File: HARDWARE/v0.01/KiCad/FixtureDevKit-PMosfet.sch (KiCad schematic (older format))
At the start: 56 parts, among them J89 FET_0, J90 FET_1, J91 FET_2, J92 FET_3, J93 FET_4, J94 FET_5, J95 FET_6, J96 FET_7, Q10 NTF2955T1G, Q11 NTF2955T1G, Q12 NTF2955T1G, Q5 NTF2955T1G, Q6 NTF2955T1G, Q7 NTF2955T1G, Q8 NTF2955T1G, Q9 NTF2955T1G

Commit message: adjusting page sizes and cleaning up schematics
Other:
- moved on the sheet: J89, J90, J91, J92, J93, J94, J95, J96, Q10, Q11, Q12, Q5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

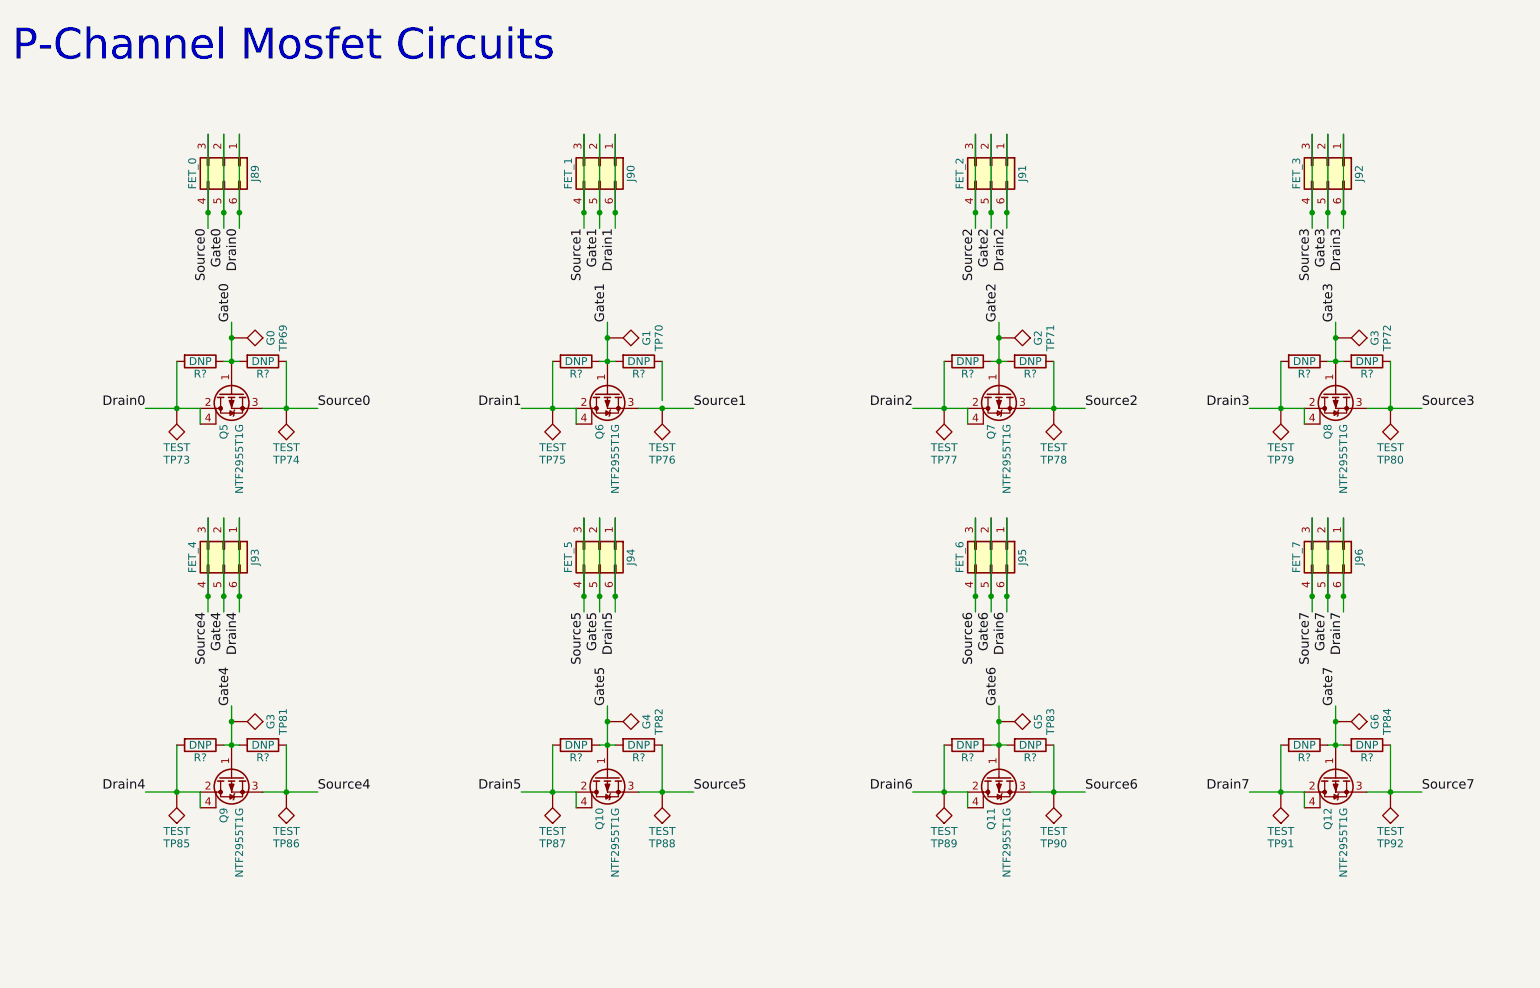
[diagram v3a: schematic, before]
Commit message: cleaning up schematic, run rules check, generate net list
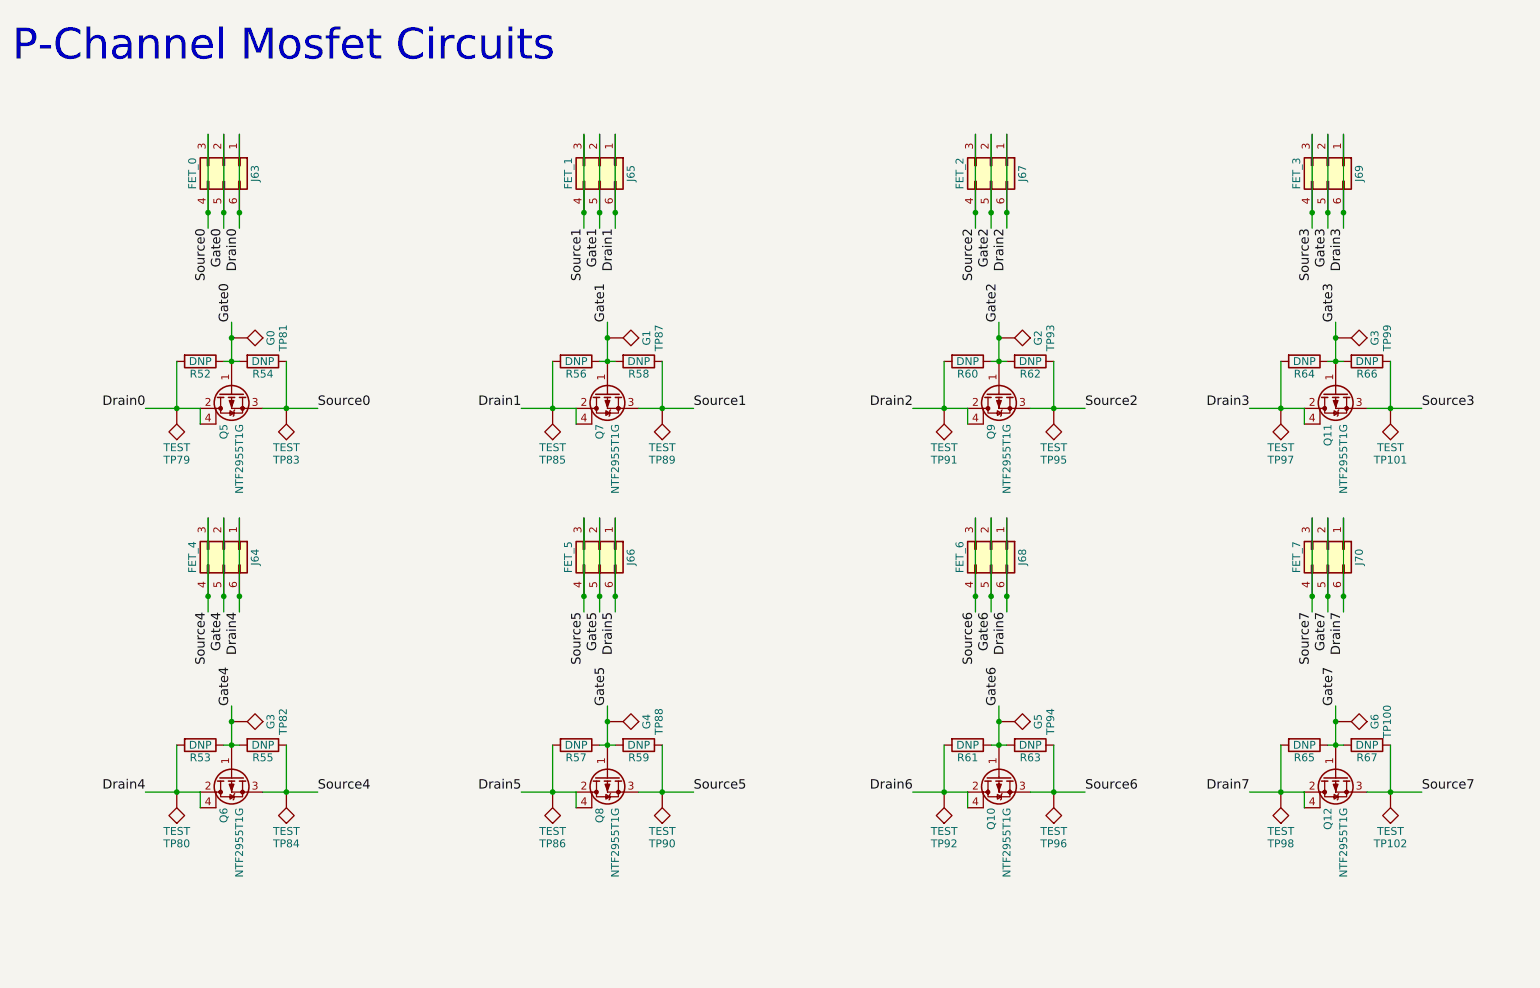
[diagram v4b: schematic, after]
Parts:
- gave numbers to parts that had none: 16
- renumbered J89 to J63, J93 to J64, J90 to J65, J94 to J66, J91 to J67, J95 to J68, J92 to J69, J96 to J70, Q11 to Q10, Q8 to Q11, Q9 to Q6, Q6 to Q7, Q10 to Q8, Q7 to Q9, TP84 to TP100, TP80 to TP101, TP92 to TP102, TP73 to TP79, TP85 to TP80, TP69 to TP81, TP81 to TP82, TP74 to TP83, TP86 to TP84, TP75 to TP85, TP87 to TP86, TP70 to TP87, TP82 to TP88, TP76 to TP89, TP88 to TP90, TP77 to TP91, TP89 to TP92, TP71 to TP93, TP83 to TP94, TP78 to TP95, TP90 to TP96, TP79 to TP97, TP91 to TP98, TP72 to TP99
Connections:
- net Source1: now also R58.1

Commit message: adding footprints
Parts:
- J63, J64, J65, J66, J67, J68, J69, J70: footprint (none) -> Pin_Headers:Pin_Header_Straight_2x03_Pitch2.54mm
- Q10, Q11, Q12, Q5, Q6, Q7, Q8, Q9: footprint (none) -> Pin_Headers:Pin_Header_Straight_1x04_Pitch2.54mm
- R52, R53, R54, R55, R56, R57, R58, R59, R60, R61, R62, R63, R64, R65, R66, R67: footprint (none) -> Resistors_SMD:R_0805_HandSoldering
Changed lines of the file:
@@
 F 0 "R67" V 9330 5150 50  0000 C CNN
 F 1 "DNP" V 9250 5150 50  0000 C CNN
-F 2 "" V 9180 5150 50  0001 C CNN
+F 2 "Resistors_SMD:R_0805_HandSoldering" V 9180 5150 50  0001 C CNN
 F 3 "" H 9250 5150 50  0001 C CNN
 	1    9250 5150
@@
 F 0 "R65" V 8930 5150 50  0000 C CNN
 F 1 "DNP" V 8850 5150 50  0000 C CNN
-F 2 "" V 8780 5150 50  0001 C CNN
+F 2 "Resistors_SMD:R_0805_HandSoldering" V 8780 5150 50  0001 C CNN
 F 3 "" H 8850 5150 50  0001 C CNN
 	1    8850 5150
@@
 F 0 "R61" V 6780 5150 50  0000 C CNN
 F 1 "DNP" V 6700 5150 50  0000 C CNN
-F 2 "" V 6630 5150 50  0001 C CNN
+F 2 "Resistors_SMD:R_0805_HandSoldering" V 6630 5150 50  0001 C CNN
 F 3 "" H 6700 5150 50  0001 C CNN
 	1    6700 5150
@@
 F 0 "R63" V 7180 5150 50  0000 C CNN
 F 1 "DNP" V 7100 5150 50  0000 C CNN
-F 2 "" V 7030 5150 50  0001 C CNN
+F 2 "Resistors_SMD:R_0805_HandSoldering" V 7030 5150 50  0001 C CNN
 F 3 "" H 7100 5150 50  0001 C CNN
 	1    7100 5150
@@
 F 0 "R59" V 4680 5150 50  0000 C CNN
 F 1 "DNP" V 4600 5150 50  0000 C CNN
-F 2 "" V 4530 5150 50  0001 C CNN
+F 2 "Resistors_SMD:R_0805_HandSoldering" V 4530 5150 50  0001 C CNN
 F 3 "" H 4600 5150 50  0001 C CNN
 	1    4600 5150
@@
 F 0 "R57" V 4280 5150 50  0000 C CNN
 F 1 "DNP" V 4200 5150 50  0000 C CNN
-F 2 "" V 4130 5150 50  0001 C CNN
+F 2 "Resistors_SMD:R_0805_HandSoldering" V 4130 5150 50  0001 C CNN
 F 3 "" H 4200 5150 50  0001 C CNN
 	1    4200 5150
@@
 F 0 "R53" V 1880 5150 50  0000 C CNN
 F 1 "DNP" V 1800 5150 50  0000 C CNN
-F 2 "" V 1730 5150 50  0001 C CNN
+F 2 "Resistors_SMD:R_0805_HandSoldering" V 1730 5150 50  0001 C CNN
 F 3 "" H 1800 5150 50  0001 C CNN
 	1    1800 5150
@@
 F 0 "R55" V 2280 5150 50  0000 C CNN
 F 1 "DNP" V 2200 5150 50  0000 C CNN
-F 2 "" V 2130 5150 50  0001 C CNN
+F 2 "Resistors_SMD:R_0805_HandSoldering" V 2130 5150 50  0001 C CNN
 F 3 "" H 2200 5150 50  0001 C CNN
 	1    2200 5150
@@
 F 0 "R66" V 9330 2700 50  0000 C CNN
 F 1 "DNP" V 9250 2700 50  0000 C CNN
-F 2 "" V 9180 2700 50  0001 C CNN
+F 2 "Resistors_SMD:R_0805_HandSoldering" V 9180 2700 50  0001 C CNN
 F 3 "" H 9250 2700 50  0001 C CNN
 	1    9250 2700
@@
 F 0 "R64" V 8930 2700 50  0000 C CNN
 F 1 "DNP" V 8850 2700 50  0000 C CNN
-F 2 "" V 8780 2700 50  0001 C CNN
+F 2 "Resistors_SMD:R_0805_HandSoldering" V 8780 2700 50  0001 C CNN
 F 3 "" H 8850 2700 50  0001 C CNN
 	1    8850 2700
@@
 F 0 "R62" V 7180 2700 50  0000 C CNN
 F 1 "DNP" V 7100 2700 50  0000 C CNN
-F 2 "" V 7030 2700 50  0001 C CNN
+F 2 "Resistors_SMD:R_0805_HandSoldering" V 7030 2700 50  0001 C CNN
 F 3 "" H 7100 2700 50  0001 C CNN
 	1    7100 2700
@@
 F 0 "R60" V 6780 2700 50  0000 C CNN
 F 1 "DNP" V 6700 2700 50  0000 C CNN
-F 2 "" V 6630 2700 50  0001 C CNN
+F 2 "Resistors_SMD:R_0805_HandSoldering" V 6630 2700 50  0001 C CNN
 F 3 "" H 6700 2700 50  0001 C CNN
 	1    6700 2700
@@
 F 0 "R56" V 4280 2700 50  0000 C CNN
 F 1 "DNP" V 4200 2700 50  0000 C CNN
-F 2 "" V 4130 2700 50  0001 C CNN
+F 2 "Resistors_SMD:R_0805_HandSoldering" V 4130 2700 50  0001 C CNN
 F 3 "" H 4200 2700 50  0001 C CNN
 	1    4200 2700
@@
 F 0 "R58" V 4680 2700 50  0000 C CNN
 F 1 "DNP" V 4600 2700 50  0000 C CNN
-F 2 "" V 4530 2700 50  0001 C CNN
+F 2 "Resistors_SMD:R_0805_HandSoldering" V 4530 2700 50  0001 C CNN
 F 3 "" H 4600 2700 50  0001 C CNN
 	1    4600 2700
@@
 F 0 "R52" V 1880 2700 50  0000 C CNN
 F 1 "DNP" V 1800 2700 50  0000 C CNN
-F 2 "" V 1730 2700 50  0001 C CNN
+F 2 "Resistors_SMD:R_0805_HandSoldering" V 1730 2700 50  0001 C CNN
 F 3 "" H 1800 2700 50  0001 C CNN
 	1    1800 2700
@@
 F 0 "R54" V 2280 2700 50  0000 C CNN
 F 1 "DNP" V 2200 2700 50  0000 C CNN
-F 2 "" V 2130 2700 50  0001 C CNN
+F 2 "Resistors_SMD:R_0805_HandSoldering" V 2130 2700 50  0001 C CNN
 F 3 "" H 2200 2700 50  0001 C CNN
 	1    2200 2700
@@
 F 0 "J70" H 9050 4100 50  0000 C CNN
 F 1 "FET_7" H 9050 3700 50  0000 C CNN
-F 2 "" H 9000 3900 50  0001 C CNN
+F 2 "Pin_Headers:Pin_Header_Straight_2x03_Pitch2.54mm" H 9000 3900 50  0001 C CNN
 F 3 "" H 9000 3900 50  0001 C CNN
 	1    9000 3900
@@
 F 0 "Q12" H 9250 5400 50  0000 L CNN
 F 1 "NTF2955T1G" H 9250 5300 50  0000 L CNN
-F 2 "" H 9250 5450 50  0001 C CNN
+F 2 "Pin_Headers:Pin_Header_Straight_1x04_Pitch2.54mm" H 9250 5450 50  0001 C CNN
 F 3 "" H 9050 5350 50  0001 C CNN
 	1    9050 5350
@@
 F 0 "J68" H 6900 4100 50  0000 C CNN
 F 1 "FET_6" H 6900 3700 50  0000 C CNN
-F 2 "" H 6850 3900 50  0001 C CNN
+F 2 "Pin_Headers:Pin_Header_Straight_2x03_Pitch2.54mm" H 6850 3900 50  0001 C CNN
 F 3 "" H 6850 3900 50  0001 C CNN
 	1    6850 3900
@@
 F 0 "Q10" H 7100 5400 50  0000 L CNN
 F 1 "NTF2955T1G" H 7100 5300 50  0000 L CNN
-F 2 "" H 7100 5450 50  0001 C CNN
+F 2 "Pin_Headers:Pin_Header_Straight_1x04_Pitch2.54mm" H 7100 5450 50  0001 C CNN
 F 3 "" H 6900 5350 50  0001 C CNN
 	1    6900 5350
@@
 F 0 "J66" H 4400 4100 50  0000 C CNN
 F 1 "FET_5" H 4400 3700 50  0000 C CNN
-F 2 "" H 4350 3900 50  0001 C CNN
+F 2 "Pin_Headers:Pin_Header_Straight_2x03_Pitch2.54mm" H 4350 3900 50  0001 C CNN
 F 3 "" H 4350 3900 50  0001 C CNN
 	1    4350 3900
@@
 F 0 "Q8" H 4600 5400 50  0000 L CNN
 F 1 "NTF2955T1G" H 4600 5300 50  0000 L CNN
-F 2 "" H 4600 5450 50  0001 C CNN
+F 2 "Pin_Headers:Pin_Header_Straight_1x04_Pitch2.54mm" H 4600 5450 50  0001 C CNN
 F 3 "" H 4400 5350 50  0001 C CNN
 	1    4400 5350
@@
 F 0 "J64" H 2000 4100 50  0000 C CNN
 F 1 "FET_4" H 2000 3700 50  0000 C CNN
-F 2 "" H 1950 3900 50  0001 C CNN
+F 2 "Pin_Headers:Pin_Header_Straight_2x03_Pitch2.54mm" H 1950 3900 50  0001 C CNN
 F 3 "" H 1950 3900 50  0001 C CNN
 	1    1950 3900
@@
 F 0 "Q6" H 2200 5400 50  0000 L CNN
 F 1 "NTF2955T1G" H 2200 5300 50  0000 L CNN
-F 2 "" H 2200 5450 50  0001 C CNN
+F 2 "Pin_Headers:Pin_Header_Straight_1x04_Pitch2.54mm" H 2200 5450 50  0001 C CNN
 F 3 "" H 2000 5350 50  0001 C CNN
 	1    2000 5350
@@
 F 0 "J69" H 9050 1650 50  0000 C CNN
 F 1 "FET_3" H 9050 1250 50  0000 C CNN
-F 2 "" H 9000 1450 50  0001 C CNN
+F 2 "Pin_Headers:Pin_Header_Straight_2x03_Pitch2.54mm" H 9000 1450 50  0001 C CNN
 F 3 "" H 9000 1450 50  0001 C CNN
 	1    9000 1450
@@
 F 0 "Q11" H 9250 2950 50  0000 L CNN
 F 1 "NTF2955T1G" H 9250 2850 50  0000 L CNN
-F 2 "" H 9250 3000 50  0001 C CNN
+F 2 "Pin_Headers:Pin_Header_Straight_1x04_Pitch2.54mm" H 9250 3000 50  0001 C CNN
 F 3 "" H 9050 2900 50  0001 C CNN
 	1    9050 2900
@@
 F 0 "J67" H 6900 1650 50  0000 C CNN
 F 1 "FET_2" H 6900 1250 50  0000 C CNN
-F 2 "" H 6850 1450 50  0001 C CNN
+F 2 "Pin_Headers:Pin_Header_Straight_2x03_Pitch2.54mm" H 6850 1450 50  0001 C CNN
 F 3 "" H 6850 1450 50  0001 C CNN
 	1    6850 1450
@@
 F 0 "Q9" H 7100 2950 50  0000 L CNN
 F 1 "NTF2955T1G" H 7100 2850 50  0000 L CNN
-F 2 "" H 7100 3000 50  0001 C CNN
+F 2 "Pin_Headers:Pin_Header_Straight_1x04_Pitch2.54mm" H 7100 3000 50  0001 C CNN
 F 3 "" H 6900 2900 50  0001 C CNN
 	1    6900 2900
@@
 F 0 "J65" H 4400 1650 50  0000 C CNN
 F 1 "FET_1" H 4400 1250 50  0000 C CNN
-F 2 "" H 4350 1450 50  0001 C CNN
+F 2 "Pin_Headers:Pin_Header_Straight_2x03_Pitch2.54mm" H 4350 1450 50  0001 C CNN
 F 3 "" H 4350 1450 50  0001 C CNN
 	1    4350 1450
@@
 F 0 "Q7" H 4600 2950 50  0000 L CNN
 F 1 "NTF2955T1G" H 4600 2850 50  0000 L CNN
-F 2 "" H 4600 3000 50  0001 C CNN
+F 2 "Pin_Headers:Pin_Header_Straight_1x04_Pitch2.54mm" H 4600 3000 50  0001 C CNN
 F 3 "" H 4400 2900 50  0001 C CNN
 	1    4400 2900
@@
 F 0 "J63" H 2000 1650 50  0000 C CNN
 F 1 "FET_0" H 2000 1250 50  0000 C CNN
-F 2 "" H 1950 1450 50  0001 C CNN
+F 2 "Pin_Headers:Pin_Header_Straight_2x03_Pitch2.54mm" H 1950 1450 50  0001 C CNN
 F 3 "" H 1950 1450 50  0001 C CNN
 	1    1950 1450
@@
 F 0 "Q5" H 2200 2950 50  0000 L CNN
 F 1 "NTF2955T1G" H 2200 2850 50  0000 L CNN
-F 2 "" H 2200 3000 50  0001 C CNN
+F 2 "Pin_Headers:Pin_Header_Straight_1x04_Pitch2.54mm" H 2200 3000 50  0001 C CNN
 F 3 "" H 2000 2900 50  0001 C CNN
 	1    2000 2900

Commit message: adding footprints, starting layout
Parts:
- Q10, Q11, Q12, Q5, Q6, Q7, Q8, Q9: footprint Pin_Headers:Pin_Header_Straight_1x04_Pitch2.54mm -> TO_SOT_Packages_SMD:SOT-223
- TP100, TP101, TP102, TP79, TP80, TP81, TP82, TP83, TP84, TP85, TP86, TP87, TP88, TP89, TP90, TP91, TP92, TP93, TP94, TP95, TP96, TP97, TP98, TP99: footprint (none) -> TestPoint:TestPoint
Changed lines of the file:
@@
 LIBS:contrib
 LIBS:valves
-LIBS:FDN337N
+LIBS:TCA6424ARGJR
 LIBS:Fixture-Dev-Kit-cache
 EELAYER 25 0
@@
 F 0 "TP98" H 8700 5750 50  0000 C BNN
 F 1 "TEST" H 8700 5700 50  0000 C CNN
-F 2 "" H 8700 5450 50  0001 C CNN
+F 2 "TestPoint:TestPoint" H 8700 5450 50  0001 C CNN
 F 3 "" H 8700 5450 50  0001 C CNN
 	1    8700 5450
@@
 F 0 "TP102" H 9400 5750 50  0000 C BNN
 F 1 "TEST" H 9400 5700 50  0000 C CNN
-F 2 "" H 9400 5450 50  0001 C CNN
+F 2 "TestPoint:TestPoint" H 9400 5450 50  0001 C CNN
 F 3 "" H 9400 5450 50  0001 C CNN
 	1    9400 5450
@@
 F 0 "TP100" H 9050 5300 50  0000 C BNN
 F 1 "G6" H 9050 5250 50  0000 C CNN
-F 2 "" H 9050 5000 50  0001 C CNN
+F 2 "TestPoint:TestPoint" H 9050 5000 50  0001 C CNN
 F 3 "" H 9050 5000 50  0001 C CNN
 	1    9050 5000
@@
 F 0 "Q12" H 9250 5400 50  0000 L CNN
 F 1 "NTF2955T1G" H 9250 5300 50  0000 L CNN
-F 2 "Pin_Headers:Pin_Header_Straight_1x04_Pitch2.54mm" H 9250 5450 50  0001 C CNN
+F 2 "TO_SOT_Packages_SMD:SOT-223" H 9250 5450 50  0001 C CNN
 F 3 "" H 9050 5350 50  0001 C CNN
 	1    9050 5350
@@
 F 0 "TP92" H 6550 5750 50  0000 C BNN
 F 1 "TEST" H 6550 5700 50  0000 C CNN
-F 2 "" H 6550 5450 50  0001 C CNN
+F 2 "TestPoint:TestPoint" H 6550 5450 50  0001 C CNN
 F 3 "" H 6550 5450 50  0001 C CNN
 	1    6550 5450
@@
 F 0 "TP96" H 7250 5750 50  0000 C BNN
 F 1 "TEST" H 7250 5700 50  0000 C CNN
-F 2 "" H 7250 5450 50  0001 C CNN
+F 2 "TestPoint:TestPoint" H 7250 5450 50  0001 C CNN
 F 3 "" H 7250 5450 50  0001 C CNN
 	1    7250 5450
@@
 F 0 "TP94" H 6900 5300 50  0000 C BNN
 F 1 "G5" H 6900 5250 50  0000 C CNN
-F 2 "" H 6900 5000 50  0001 C CNN
+F 2 "TestPoint:TestPoint" H 6900 5000 50  0001 C CNN
 F 3 "" H 6900 5000 50  0001 C CNN
 	1    6900 5000
@@
 F 0 "Q10" H 7100 5400 50  0000 L CNN
 F 1 "NTF2955T1G" H 7100 5300 50  0000 L CNN
-F 2 "Pin_Headers:Pin_Header_Straight_1x04_Pitch2.54mm" H 7100 5450 50  0001 C CNN
+F 2 "TO_SOT_Packages_SMD:SOT-223" H 7100 5450 50  0001 C CNN
 F 3 "" H 6900 5350 50  0001 C CNN
 	1    6900 5350
@@
 F 0 "TP86" H 4050 5750 50  0000 C BNN
 F 1 "TEST" H 4050 5700 50  0000 C CNN
-F 2 "" H 4050 5450 50  0001 C CNN
+F 2 "TestPoint:TestPoint" H 4050 5450 50  0001 C CNN
 F 3 "" H 4050 5450 50  0001 C CNN
 	1    4050 5450
@@
 F 0 "TP90" H 4750 5750 50  0000 C BNN
 F 1 "TEST" H 4750 5700 50  0000 C CNN
-F 2 "" H 4750 5450 50  0001 C CNN
+F 2 "TestPoint:TestPoint" H 4750 5450 50  0001 C CNN
 F 3 "" H 4750 5450 50  0001 C CNN
 	1    4750 5450
@@
 F 0 "TP88" H 4400 5300 50  0000 C BNN
 F 1 "G4" H 4400 5250 50  0000 C CNN
-F 2 "" H 4400 5000 50  0001 C CNN
+F 2 "TestPoint:TestPoint" H 4400 5000 50  0001 C CNN
 F 3 "" H 4400 5000 50  0001 C CNN
 	1    4400 5000
@@
 F 0 "Q8" H 4600 5400 50  0000 L CNN
 F 1 "NTF2955T1G" H 4600 5300 50  0000 L CNN
-F 2 "Pin_Headers:Pin_Header_Straight_1x04_Pitch2.54mm" H 4600 5450 50  0001 C CNN
+F 2 "TO_SOT_Packages_SMD:SOT-223" H 4600 5450 50  0001 C CNN
 F 3 "" H 4400 5350 50  0001 C CNN
 	1    4400 5350
@@
 F 0 "TP80" H 1650 5750 50  0000 C BNN
 F 1 "TEST" H 1650 5700 50  0000 C CNN
-F 2 "" H 1650 5450 50  0001 C CNN
+F 2 "TestPoint:TestPoint" H 1650 5450 50  0001 C CNN
 F 3 "" H 1650 5450 50  0001 C CNN
 	1    1650 5450
@@
 F 0 "TP84" H 2350 5750 50  0000 C BNN
 F 1 "TEST" H 2350 5700 50  0000 C CNN
-F 2 "" H 2350 5450 50  0001 C CNN
+F 2 "TestPoint:TestPoint" H 2350 5450 50  0001 C CNN
 F 3 "" H 2350 5450 50  0001 C CNN
 	1    2350 5450
@@
 F 0 "TP82" H 2000 5300 50  0000 C BNN
 F 1 "G3" H 2000 5250 50  0000 C CNN
-F 2 "" H 2000 5000 50  0001 C CNN
+F 2 "TestPoint:TestPoint" H 2000 5000 50  0001 C CNN
 F 3 "" H 2000 5000 50  0001 C CNN
 	1    2000 5000
@@
 F 0 "Q6" H 2200 5400 50  0000 L CNN
 F 1 "NTF2955T1G" H 2200 5300 50  0000 L CNN
-F 2 "Pin_Headers:Pin_Header_Straight_1x04_Pitch2.54mm" H 2200 5450 50  0001 C CNN
+F 2 "TO_SOT_Packages_SMD:SOT-223" H 2200 5450 50  0001 C CNN
 F 3 "" H 2000 5350 50  0001 C CNN
 	1    2000 5350
@@
 F 0 "TP97" H 8700 3300 50  0000 C BNN
 F 1 "TEST" H 8700 3250 50  0000 C CNN
-F 2 "" H 8700 3000 50  0001 C CNN
+F 2 "TestPoint:TestPoint" H 8700 3000 50  0001 C CNN
 F 3 "" H 8700 3000 50  0001 C CNN
 	1    8700 3000
@@
 F 0 "TP101" H 9400 3300 50  0000 C BNN
 F 1 "TEST" H 9400 3250 50  0000 C CNN
-F 2 "" H 9400 3000 50  0001 C CNN
+F 2 "TestPoint:TestPoint" H 9400 3000 50  0001 C CNN
 F 3 "" H 9400 3000 50  0001 C CNN
 	1    9400 3000
@@
 F 0 "TP99" H 9050 2850 50  0000 C BNN
 F 1 "G3" H 9050 2800 50  0000 C CNN
-F 2 "" H 9050 2550 50  0001 C CNN
+F 2 "TestPoint:TestPoint" H 9050 2550 50  0001 C CNN
 F 3 "" H 9050 2550 50  0001 C CNN
 	1    9050 2550
@@
 F 0 "Q11" H 9250 2950 50  0000 L CNN
 F 1 "NTF2955T1G" H 9250 2850 50  0000 L CNN
-F 2 "Pin_Headers:Pin_Header_Straight_1x04_Pitch2.54mm" H 9250 3000 50  0001 C CNN
+F 2 "TO_SOT_Packages_SMD:SOT-223" H 9250 3000 50  0001 C CNN
 F 3 "" H 9050 2900 50  0001 C CNN
 	1    9050 2900
@@
 F 0 "TP91" H 6550 3300 50  0000 C BNN
 F 1 "TEST" H 6550 3250 50  0000 C CNN
-F 2 "" H 6550 3000 50  0001 C CNN
+F 2 "TestPoint:TestPoint" H 6550 3000 50  0001 C CNN
 F 3 "" H 6550 3000 50  0001 C CNN
 	1    6550 3000
@@
 F 0 "TP95" H 7250 3300 50  0000 C BNN
 F 1 "TEST" H 7250 3250 50  0000 C CNN
-F 2 "" H 7250 3000 50  0001 C CNN
+F 2 "TestPoint:TestPoint" H 7250 3000 50  0001 C CNN
 F 3 "" H 7250 3000 50  0001 C CNN
 	1    7250 3000
@@
 F 0 "TP93" H 6900 2850 50  0000 C BNN
 F 1 "G2" H 6900 2800 50  0000 C CNN
-F 2 "" H 6900 2550 50  0001 C CNN
+F 2 "TestPoint:TestPoint" H 6900 2550 50  0001 C CNN
 F 3 "" H 6900 2550 50  0001 C CNN
 	1    6900 2550
@@
 F 0 "Q9" H 7100 2950 50  0000 L CNN
 F 1 "NTF2955T1G" H 7100 2850 50  0000 L CNN
-F 2 "Pin_Headers:Pin_Header_Straight_1x04_Pitch2.54mm" H 7100 3000 50  0001 C CNN
+F 2 "TO_SOT_Packages_SMD:SOT-223" H 7100 3000 50  0001 C CNN
 F 3 "" H 6900 2900 50  0001 C CNN
 	1    6900 2900
@@
 F 0 "TP85" H 4050 3300 50  0000 C BNN
 F 1 "TEST" H 4050 3250 50  0000 C CNN
-F 2 "" H 4050 3000 50  0001 C CNN
+F 2 "TestPoint:TestPoint" H 4050 3000 50  0001 C CNN
 F 3 "" H 4050 3000 50  0001 C CNN
 	1    4050 3000
@@
 F 0 "TP89" H 4750 3300 50  0000 C BNN
 F 1 "TEST" H 4750 3250 50  0000 C CNN
-F 2 "" H 4750 3000 50  0001 C CNN
+F 2 "TestPoint:TestPoint" H 4750 3000 50  0001 C CNN
 F 3 "" H 4750 3000 50  0001 C CNN
 	1    4750 3000
@@
 F 0 "TP87" H 4400 2850 50  0000 C BNN
 F 1 "G1" H 4400 2800 50  0000 C CNN
-F 2 "" H 4400 2550 50  0001 C CNN
+F 2 "TestPoint:TestPoint" H 4400 2550 50  0001 C CNN
 F 3 "" H 4400 2550 50  0001 C CNN
 	1    4400 2550
@@
 F 0 "Q7" H 4600 2950 50  0000 L CNN
 F 1 "NTF2955T1G" H 4600 2850 50  0000 L CNN
-F 2 "Pin_Headers:Pin_Header_Straight_1x04_Pitch2.54mm" H 4600 3000 50  0001 C CNN
+F 2 "TO_SOT_Packages_SMD:SOT-223" H 4600 3000 50  0001 C CNN
 F 3 "" H 4400 2900 50  0001 C CNN
 	1    4400 2900
@@
 F 0 "TP79" H 1650 3300 50  0000 C BNN
 F 1 "TEST" H 1650 3250 50  0000 C CNN
-F 2 "" H 1650 3000 50  0001 C CNN
+F 2 "TestPoint:TestPoint" H 1650 3000 50  0001 C CNN
 F 3 "" H 1650 3000 50  0001 C CNN
 	1    1650 3000
@@
 F 0 "TP83" H 2350 3300 50  0000 C BNN
 F 1 "TEST" H 2350 3250 50  0000 C CNN
-F 2 "" H 2350 3000 50  0001 C CNN
+F 2 "TestPoint:TestPoint" H 2350 3000 50  0001 C CNN
 F 3 "" H 2350 3000 50  0001 C CNN
 	1    2350 3000
@@
 F 0 "TP81" H 2000 2850 50  0000 C BNN
 F 1 "G0" H 2000 2800 50  0000 C CNN
-F 2 "" H 2000 2550 50  0001 C CNN
+F 2 "TestPoint:TestPoint" H 2000 2550 50  0001 C CNN
 F 3 "" H 2000 2550 50  0001 C CNN
 	1    2000 2550
@@
 F 0 "Q5" H 2200 2950 50  0000 L CNN
 F 1 "NTF2955T1G" H 2200 2850 50  0000 L CNN
-F 2 "Pin_Headers:Pin_Header_Straight_1x04_Pitch2.54mm" H 2200 3000 50  0001 C CNN
+F 2 "TO_SOT_Packages_SMD:SOT-223" H 2200 3000 50  0001 C CNN
 F 3 "" H 2000 2900 50  0001 C CNN
 	1    2000 2900
